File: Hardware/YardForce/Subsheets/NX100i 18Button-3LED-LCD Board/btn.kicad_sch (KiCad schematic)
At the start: 3 parts

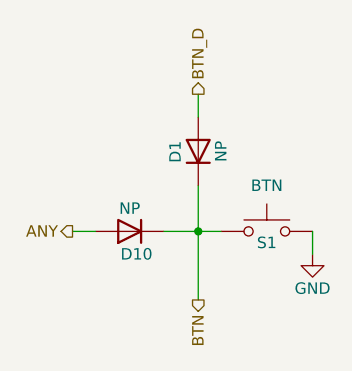
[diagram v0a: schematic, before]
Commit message: Made display a abstract Display class
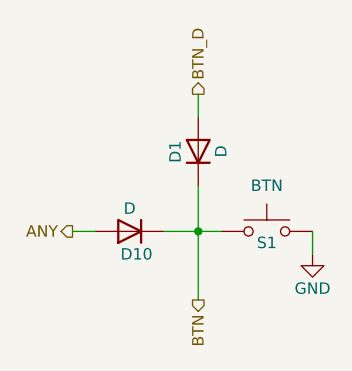
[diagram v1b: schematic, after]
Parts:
- D1, D10: value NP -> D
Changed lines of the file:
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@@
       (effects (font (size 1.27 1.27)) (justify left))
     )
-    (property "Value" "NP" (id 1) (at 124.46 88.9 0))
+    (property "Value" "D" (id 1) (at 124.46 88.9 0))
     (property "Footprint" "" (id 2) (at 124.46 91.44 0)
       (effects (font (size 1.27 1.27)) hide)
@@
       (effects (font (size 1.27 1.27)) (justify left))
     )
-    (property "Value" "NP" (id 1) (at 134.62 82.55 0))
+    (property "Value" "D" (id 1) (at 134.62 82.55 0))
     (property "Footprint" "" (id 2) (at 132.08 82.55 0)
       (effects (font (size 1.27 1.27)) hide)
